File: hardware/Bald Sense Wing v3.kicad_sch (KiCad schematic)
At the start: 48 parts, among them J1 feather long, J2 feather short, J3 1140084168, J4 STEMMA-QT, Q1 Q_PNP_BEC, Q2 Q_NPN_BEC, SW1 PTS810, U1 APDS-9960, U2 DS3231MZ, U3 SHT30-DIS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

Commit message: updated pns
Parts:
- J4: value STEMMA-QT -> JST_SH_BM04B-SRSS-TB; Field5 JST SH -> STEMMA-QT
- SW1: value PTS810 -> PTS810SJK250SMTR LFS
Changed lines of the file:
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@@
 	(text "USB Power Detection"
 		(exclude_from_sim no)
-		(at 232.156 86.106 0)
+		(at 232.156 89.916 0)
 		(effects
 			(font
@@
 			)
 		)
-		(property "Value" "STEMMA-QT"
+		(property "Value" "JST_SH_BM04B-SRSS-TB"
 			(at 217.17 85.0901 0)
 			(effects
@@
 			)
 		)
-		(property "Field5" "JST SH"
+		(property "Field5" "STEMMA-QT"
 			(at 217.17 82.5501 0)
 			(effects
@@
 			)
 		)
-		(property "Value" "PTS810"
+		(property "Value" "PTS810SJK250SMTR LFS"
 			(at 168.91 19.05 0)
 			(effects

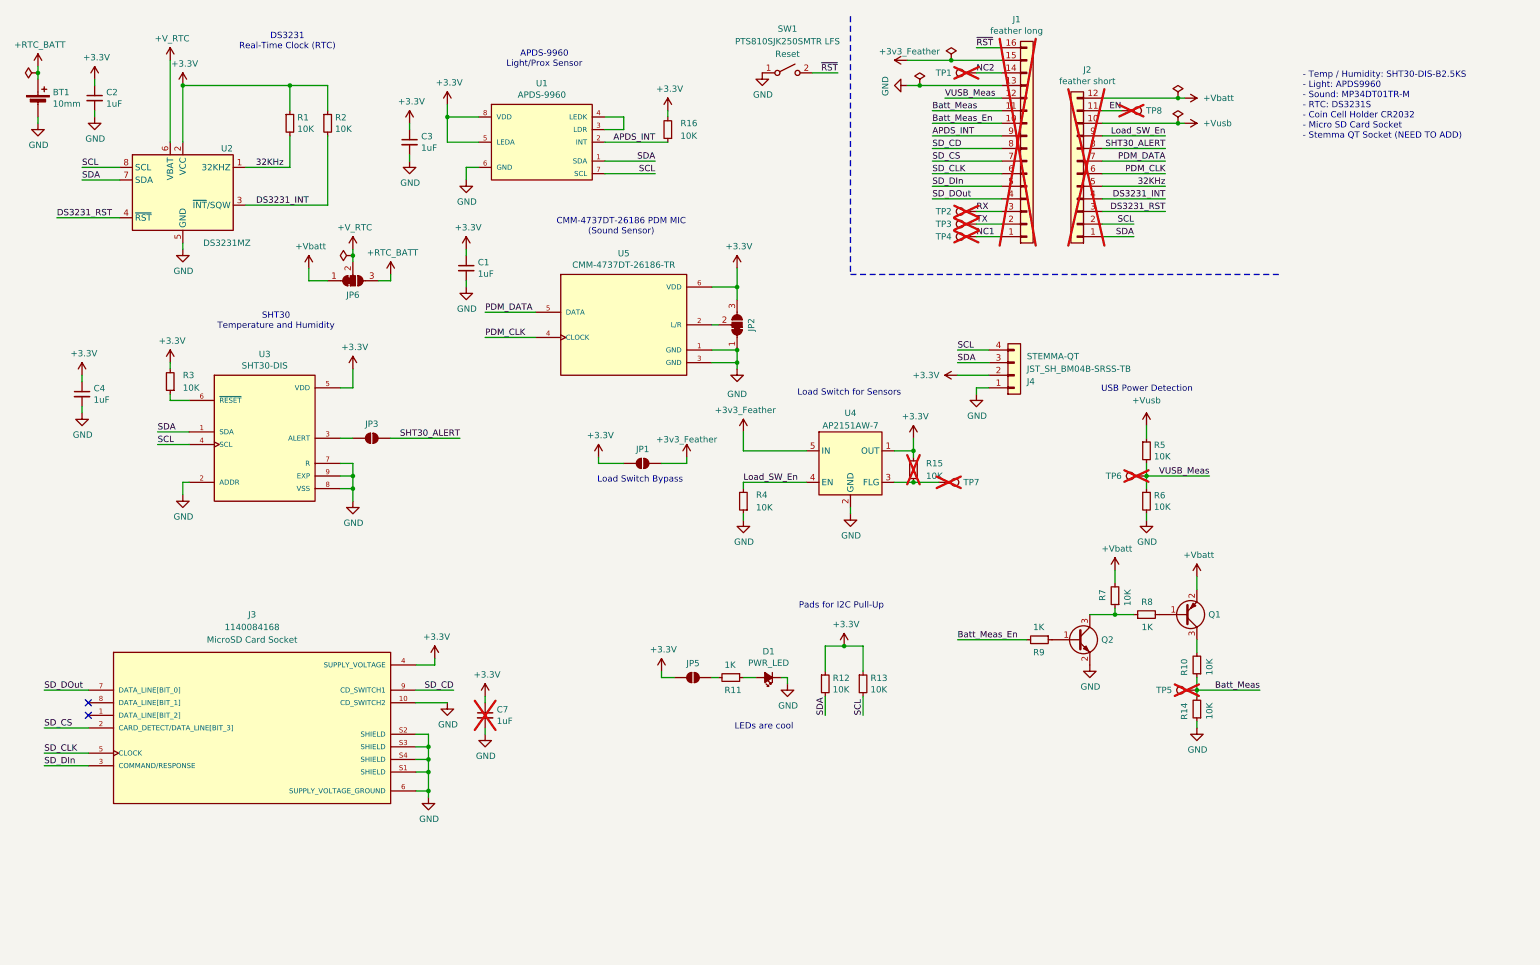
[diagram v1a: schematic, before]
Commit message: cleaned up schematic
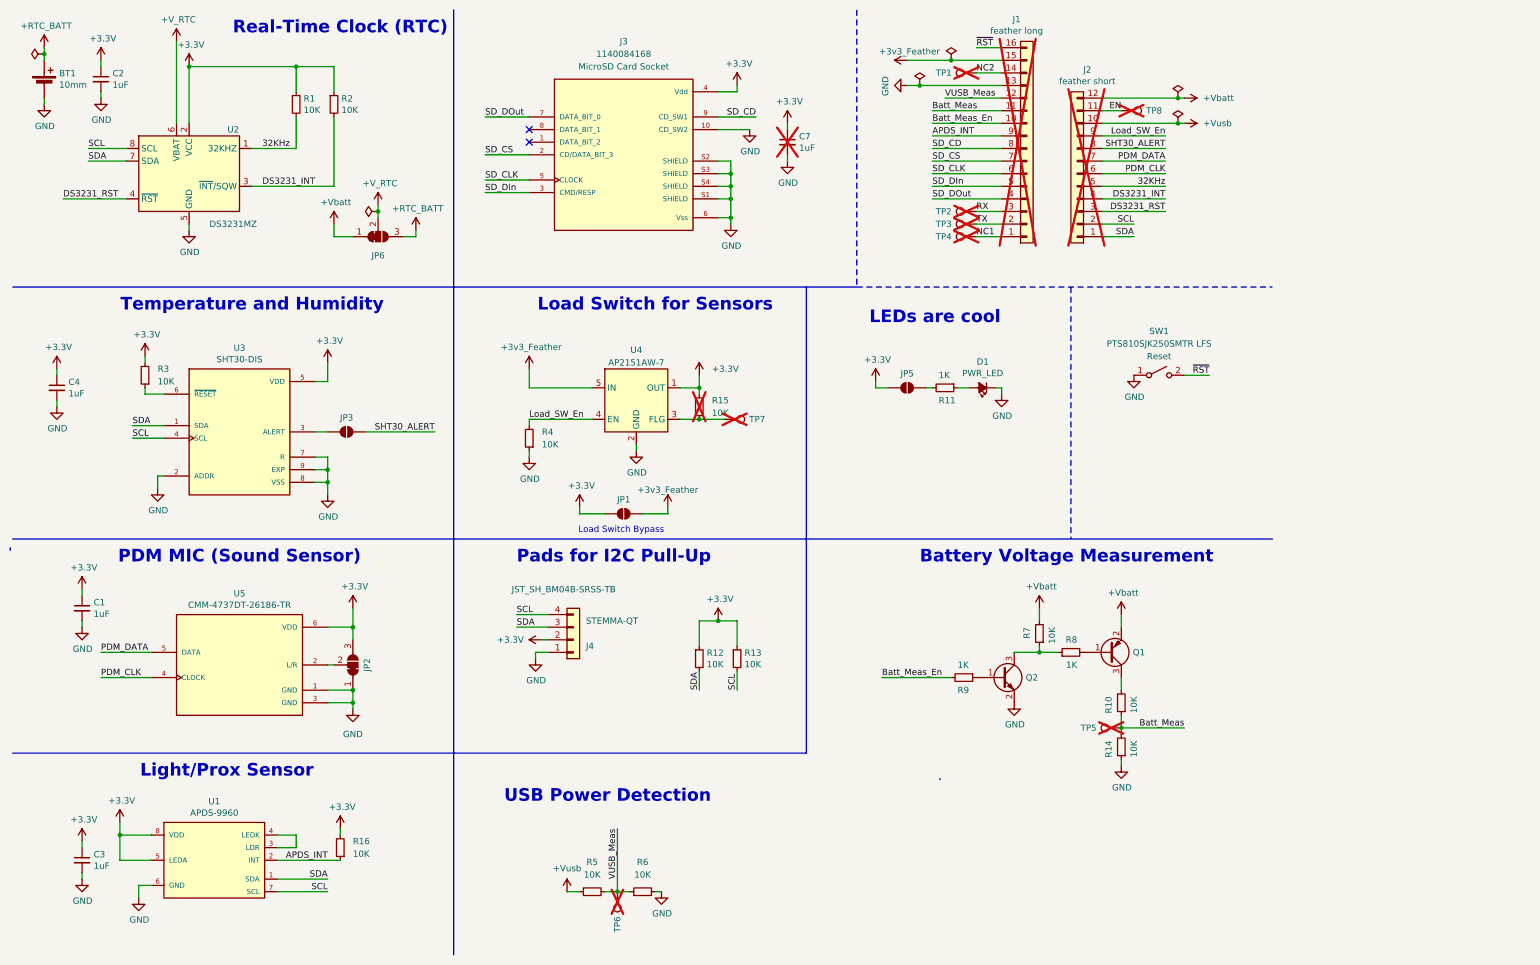
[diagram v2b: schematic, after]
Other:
- note added: "Battery Voltage Measurement"
- note added: "Light/Prox Sensor"
- note added: "PDM MIC (Sound Sensor)"
- note added: "Real-Time Clock (RTC)"
- note added: "Temperature and Humidity"
- note removed: "- Temp / Humidity: SHT30-DIS-B2.5KS - Light: APDS9960 - Sound: MP34DT01TR-M - RTC: DS3231S - Coin Cell Holder CR2032 - Micro SD Card Socket - Stemma QT Socket (NEED TO ADD)"
- note removed: "APDS-9960 Light/Prox Sensor"
- note removed: "CMM-4737DT-26186 PDM MIC (Sound Sensor)"
- note removed: "DS3231 Real-Time Clock (RTC)"
- note removed: "SHT30 Temperature and Humidity"
- moved on the sheet: BT1, C1, C2, C3, C4, C7, D1, J3, J4, JP1, JP2, JP3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

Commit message: rev3 v2 fab submit
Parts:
- added TP10, TP11, TP12, TP13, TP14, TP15, TP16, TP17, TP18, TP9: Test Point, TestPoint:TestPoint_Pad_1.0x1.0mm, symbol My Library:TestPoint_Harwin
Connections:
- net GND: now also TP16.1, TP17.1, TP18.1
- net SCL: now also TP9.1
- net SDA: now also TP10.1
- net SD_CD: now also TP15.1
- net SD_CLK: now also TP13.1
- net SD_CS: now also TP14.1
- net SD_DIn: now also TP12.1
- net SD_DOut: now also TP11.1
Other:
- title: BaldSense -> Bald SENSE
